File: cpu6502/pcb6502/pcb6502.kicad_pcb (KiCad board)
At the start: 4 copper layers, 134.6 x 96.5 mm, 38 parts, among them J1 Power, J2 RS232, J3 VIA PA, J4 VIA PB, J5 Ext RST, J6 Address, J7 Data, J8 CPU, J9 Interrupt Enable, SW1 Reset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

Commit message: forgot to save previous
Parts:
- removed J9: Interrupt Enable, Connector_PinHeader_2.54mm:PinHeader_2x06_P2.54mm_Vertical
- added SW2: IRQ Enable, Button_Switch_THT:SW_DIP_SPSTx06_Slide_6.7x16.8mm_W7.62mm_P2.54mm_LowProfile, F.Cu at (63.5, 55.9)
- U1: value 6502 (CPU) -> 6502
- U2: value 28C256 (EEPROM) -> EEPROM (28C256)
- U3: value 62256 (RAM) -> RAM (62256)
- U4: value 6522 (VIA) -> VIA (6522)
- U7: value 6551 (UART) -> ACIA (6551)
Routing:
- net /IRQ: track 55.8 -> 51.2 mm
- net /ExtNMI: track 16.2 -> 19.8 mm
- net /ExtIRQ: track 13.7 -> 16.3 mm
- net /VIAIRQ: track 81.2 -> 78.9 mm, vias 1 -> 0
- net /NMI: track 38.3 -> 36.1 mm
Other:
- board text added: "EXT"
- board text added: "Off"
- board text removed: "Ext IRQ"
- board text removed: "Ext NMI"
- board text removed: "Jmp Required for IRQ and NMI"
- board text removed: "No IRQ"
- board text removed: "No NMI"

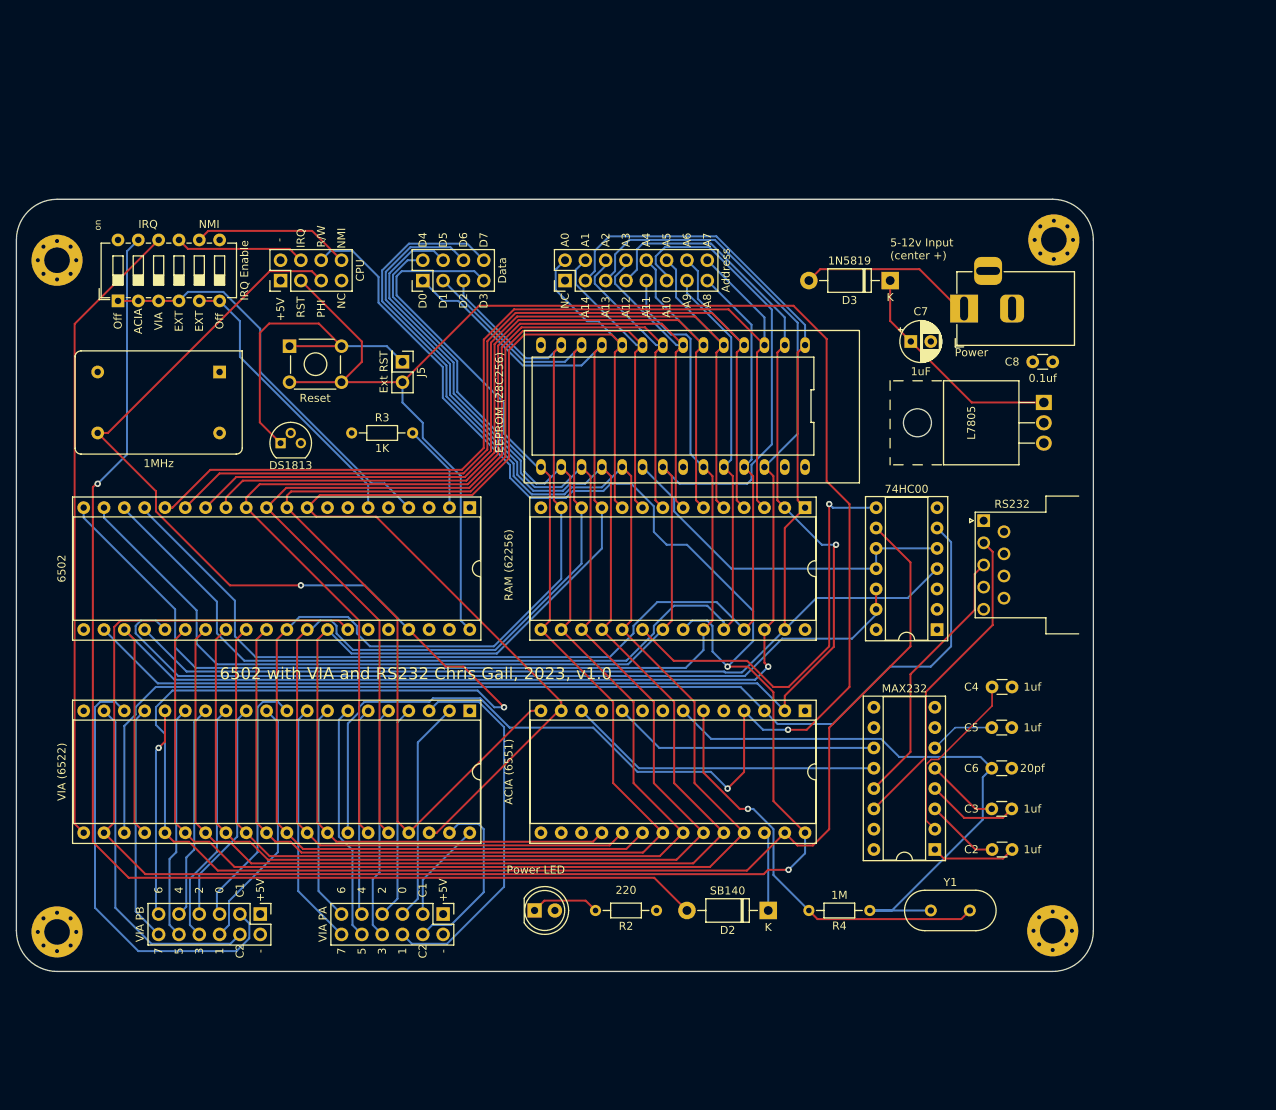
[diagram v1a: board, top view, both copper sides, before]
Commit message: pcb 6502 from 4 layers to 2 layers
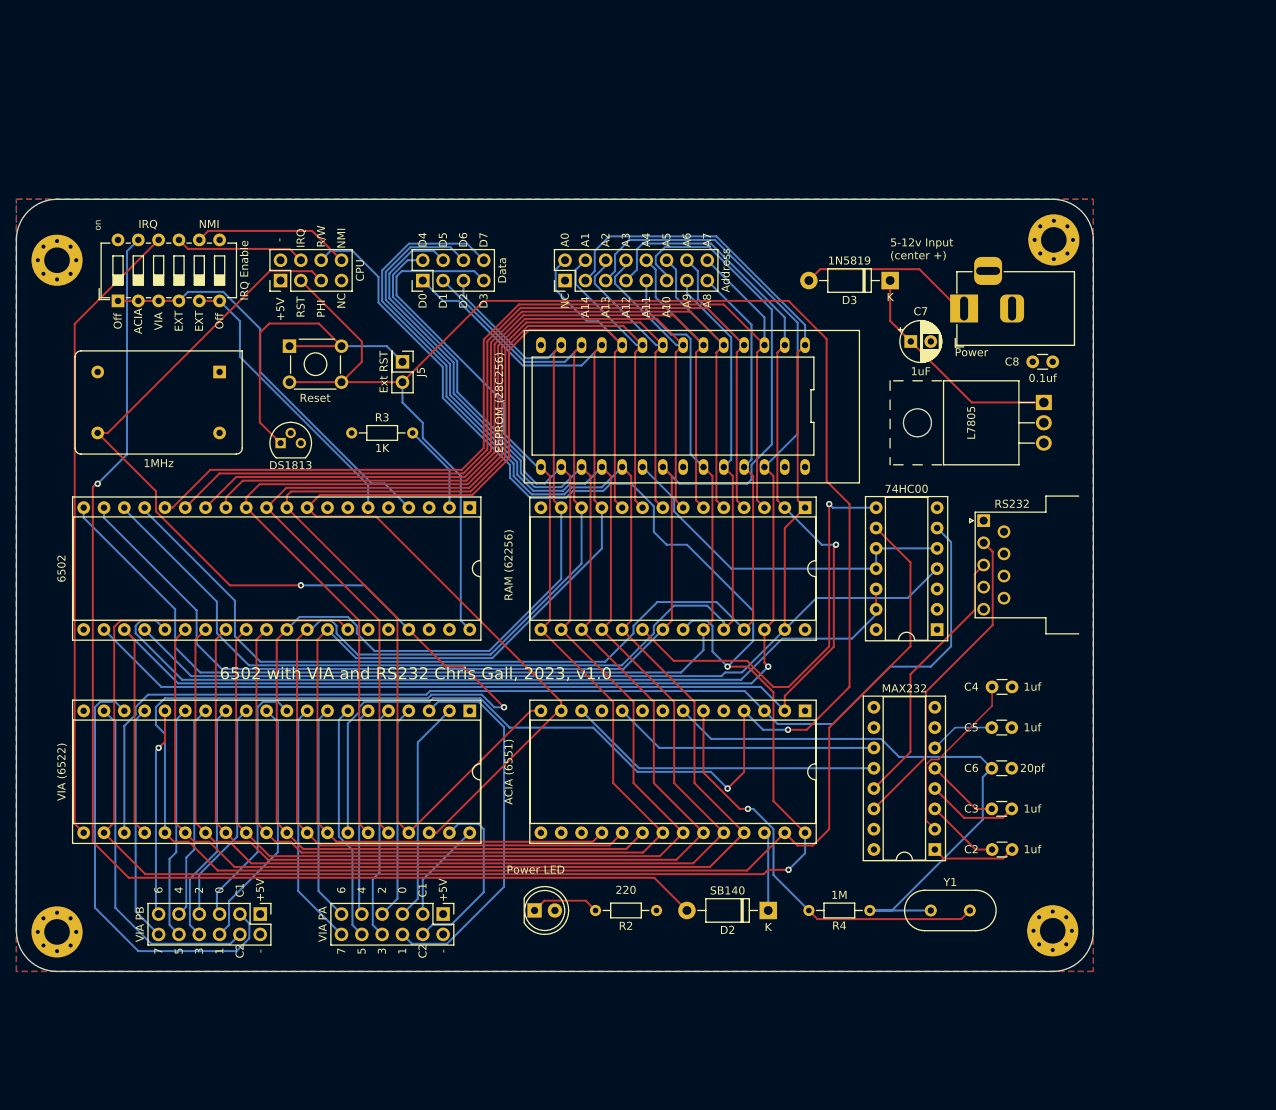
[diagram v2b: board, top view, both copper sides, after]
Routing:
- net /A3: track 157.1 -> 157.6 mm
- net /A7: track 129.6 -> 130.1 mm
- net /A4: track 114.0 -> 114.5 mm
- net /A2: track 150.9 -> 151.5 mm
- net /A0: track 159.0 -> 159.5 mm
- net /A5: track 118.7 -> 119.2 mm
- net /RST: track 263.2 -> 263.7 mm
- net /A6: track 124.2 -> 124.7 mm
- net /A1: track 169.0 -> 169.5 mm
- added copper zone on B.Cu, net +5V
- added copper zone on F.Cu, net GND
- removed copper zone on In2.Cu, net +5V
- removed copper zone on In1.Cu, net GND
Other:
- copper layers 4 -> 2

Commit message: PCB: Add RS232 RCV LED, get pours connected, CODE: checkpoint
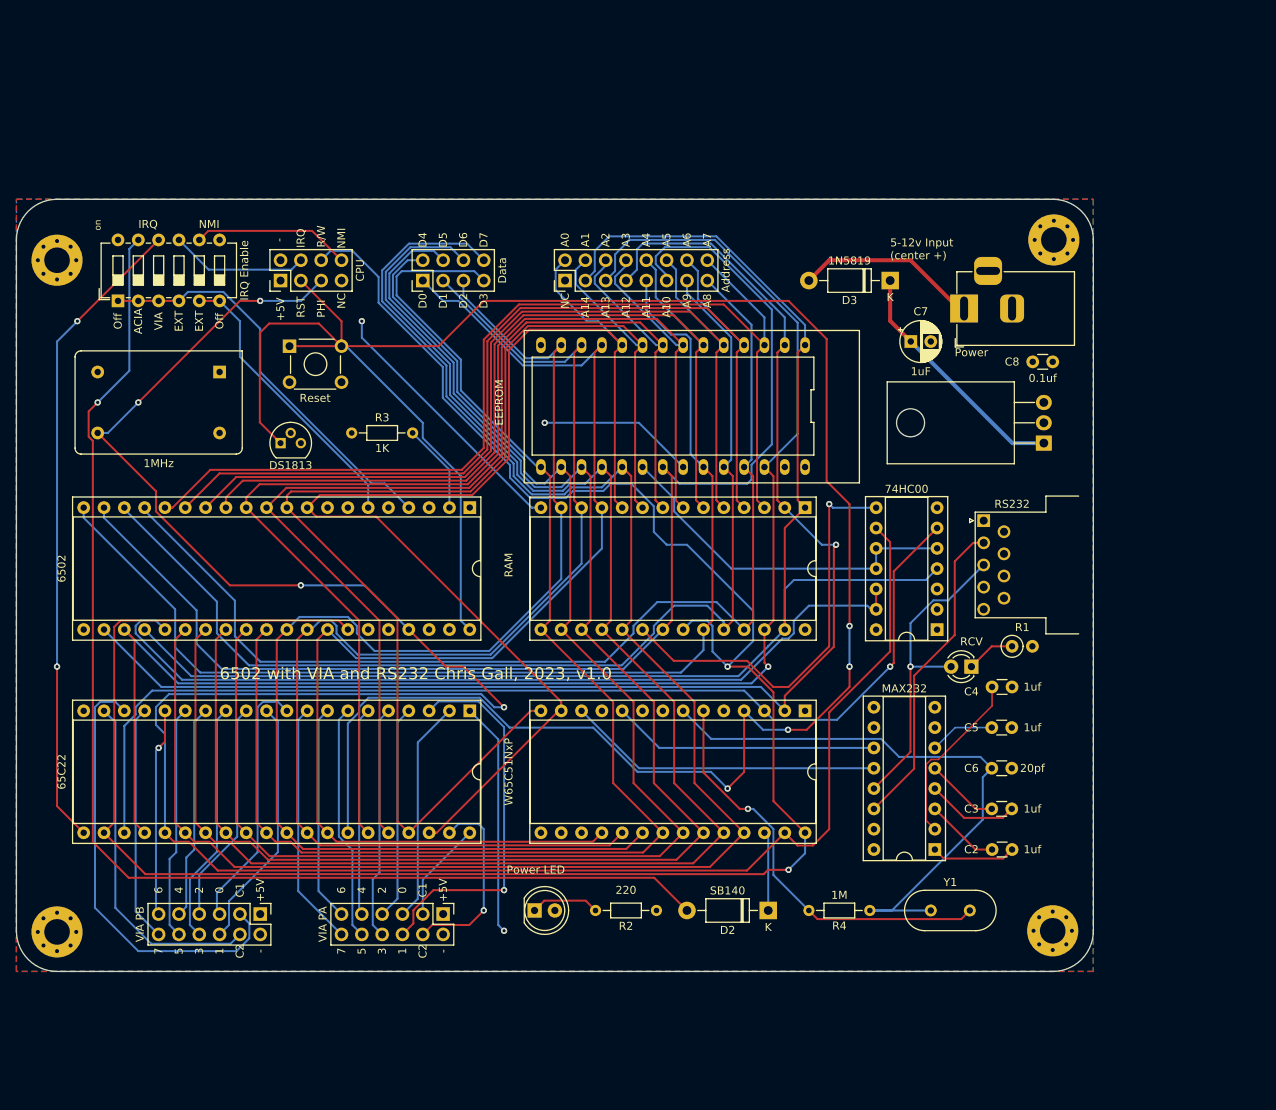
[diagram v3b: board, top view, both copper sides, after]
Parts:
- removed J5: Ext RST, Connector_PinHeader_2.54mm:PinHeader_2x01_P2.54mm_Vertical
- added D4: RCV, LED_THT:LED_D3.0mm, F.Cu at (170.2, 101.6)
- added R1: 220, Resistor_THT:R_Axial_DIN0207_L6.3mm_D2.5mm_P2.54mm_Vertical, F.Cu at (175.3, 99.1)
- U2: value EEPROM (28C256) -> EEPROM
- U3: value RAM (62256) -> RAM
- U4: value VIA (6522) -> 65C22
- U6: footprint Package_TO_SOT_THT:TO-220F-3_Horizontal_TabUp -> Package_TO_SOT_THT:TO-220-3_Horizontal_TabDown
- U7: value ACIA (6551) -> W65C51NxP
- moved U6 5.08 mm to (179.2, 73.7), turned to 90 degrees
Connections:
- SW1 pad 1: Net-(J5-Pin_1) -> /RST
- SW1 pad 2: /RST -> GND
- U9 pad 1: Net-(J5-Pin_1) -> /RST
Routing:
- net GND: track 0.00 -> 82.1 mm, vias 0 -> 3
- net Net-(J5-Pin_1): track 41.7 -> 0.00 mm
- net /RST: track 263.7 -> 290.1 mm, vias 2 -> 4
- net Net-(D4-A): track 33.6 -> 39.8 mm, vias 0 -> 1
- net Net-(D4-K): track 0.00 -> 6.13 mm
- net /CS2: track 140.3 -> 135.5 mm, vias 0 -> 1
- net /PHI2: track 296.3 -> 293.3 mm, vias 2 -> 4
- net /A14: track 182.8 -> 185.7 mm
- net Net-(D3-K): track 28.5 -> 30.6 mm
- net /A15: track 106.9 -> 108.7 mm
- net /VIAIRQ: track 78.9 -> 80.7 mm, vias 0 -> 2
- net /CA2: track 22.7 -> 24.1 mm, vias 0 -> 1
- net /ExtIRQ: track 16.3 -> 17.3 mm
- net Net-(D3-A): track 22.0 -> 23.0 mm
- net /PA1: track 47.2 -> 47.5 mm, vias 0 -> 1

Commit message: tweaks
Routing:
- net /XTAL2: track 74.7 -> 70.1 mm
- net /A15: track 108.7 -> 111.4 mm
- net /R/W: track 276.1 -> 275.3 mm

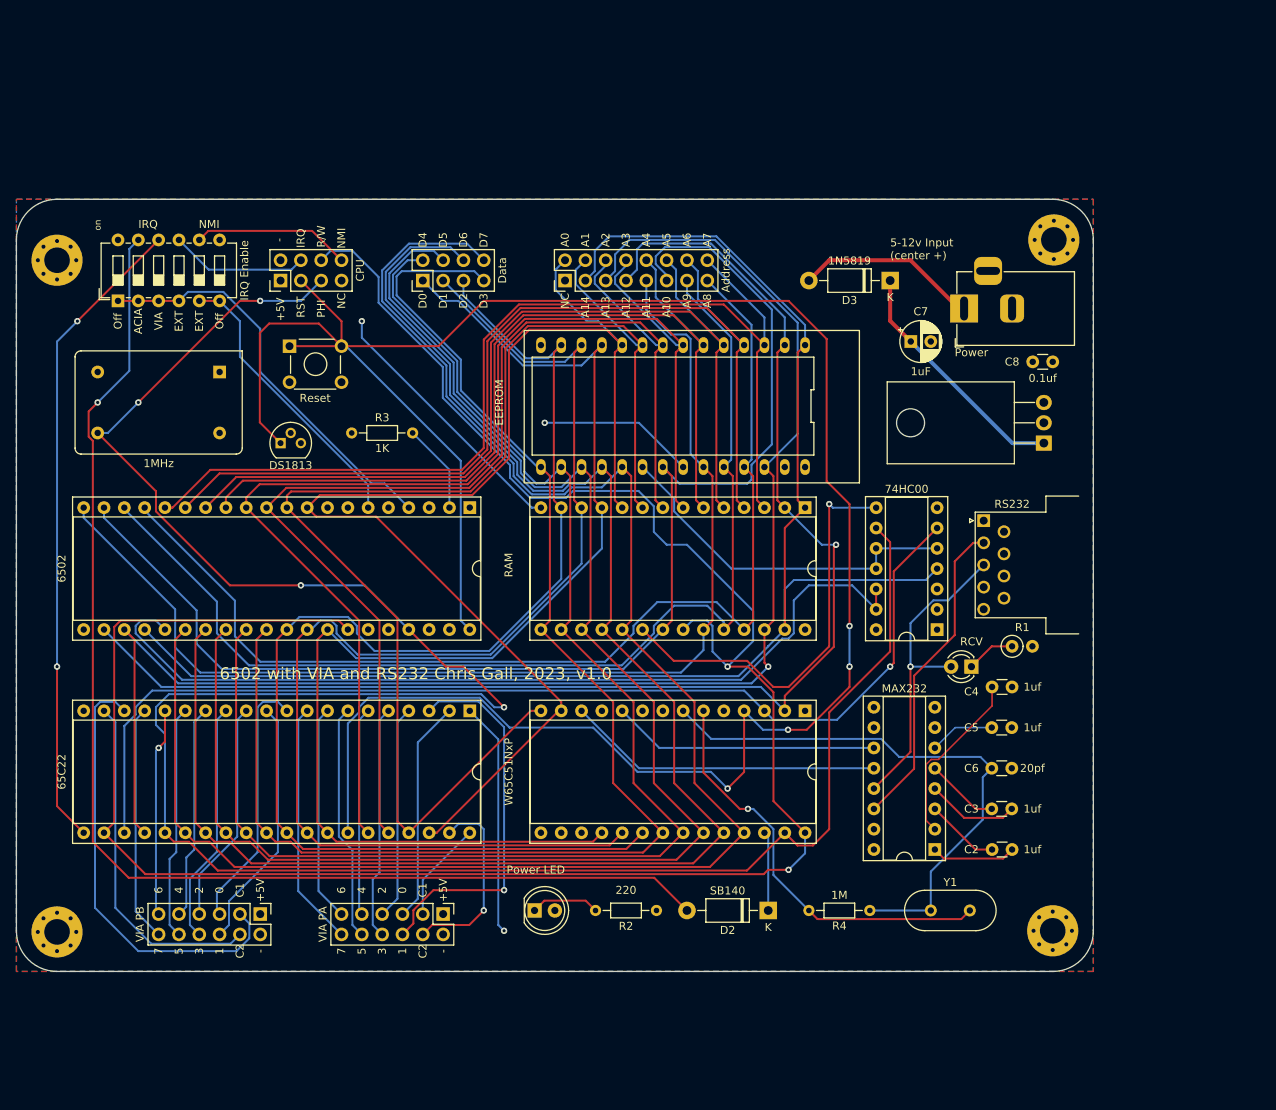
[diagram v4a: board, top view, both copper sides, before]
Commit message: update PCB with debug button, other cleanup, add Wozmon to cgOS and get it working!
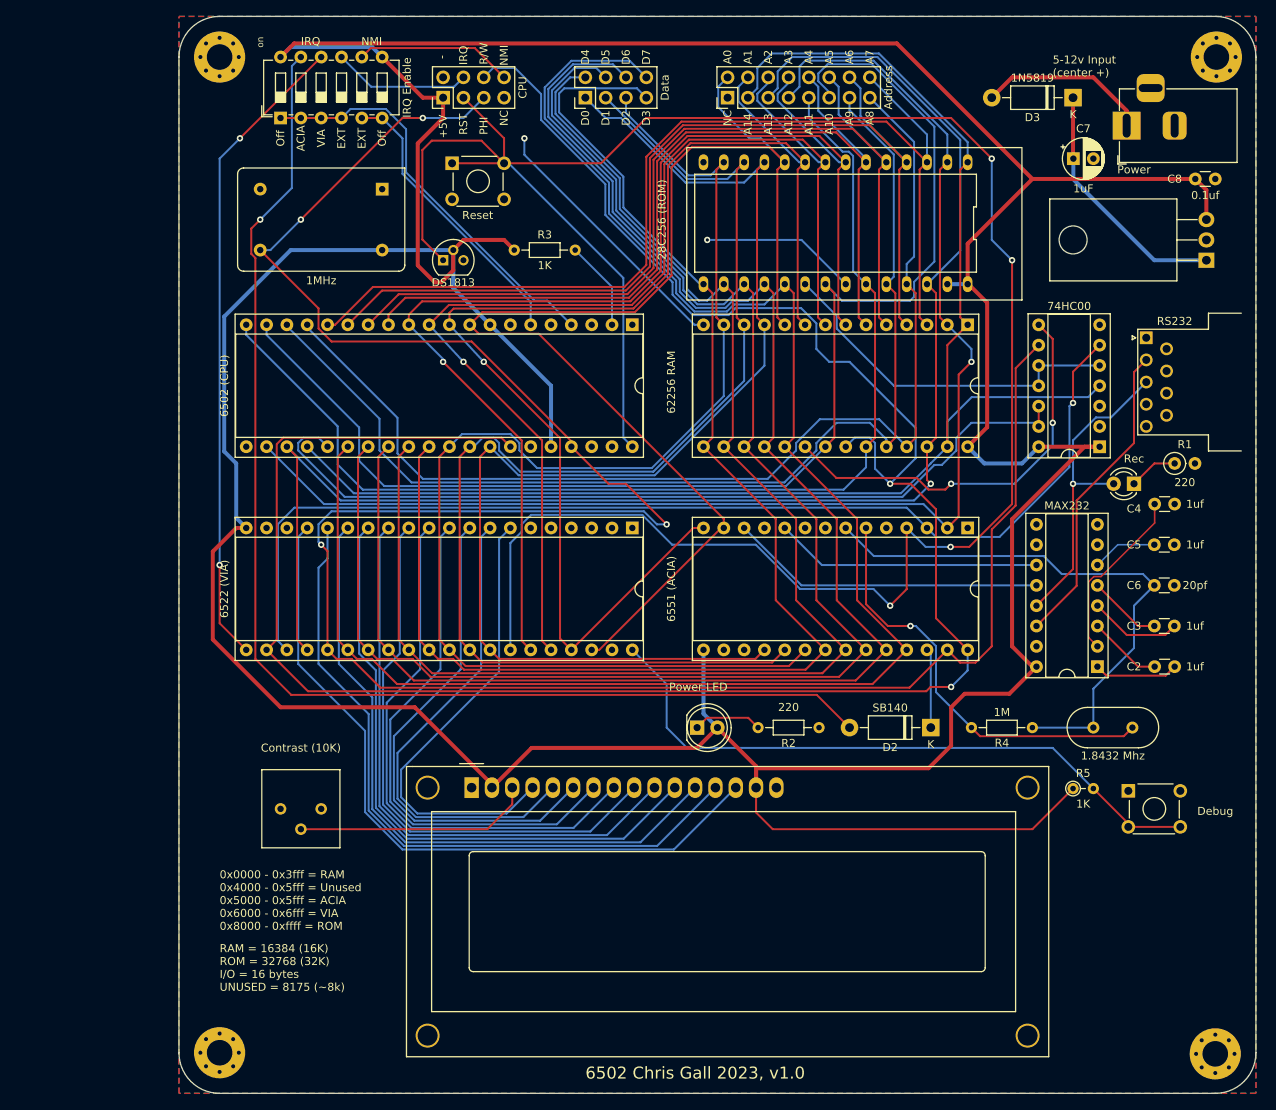
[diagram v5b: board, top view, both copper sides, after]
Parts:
- removed J3: VIA PA, Connector_PinHeader_2.54mm:PinHeader_2x06_P2.54mm_Vertical
- removed J4: VIA PB, Connector_PinHeader_2.54mm:PinHeader_2x06_P2.54mm_Vertical
- added DS1: HY1602E, Display:WC1602A, F.Cu at (107.7, 116.7)
- added R5: 1K, Resistor_THT:R_Axial_DIN0204_L3.6mm_D1.6mm_P2.54mm_Vertical, F.Cu at (182.9, 116.8)
- added RV1: Contrast (10K), Potentiometer_THT:Potentiometer_Bourns_3386P_Vertical, F.Cu at (83.8, 119.4)
- added SW3: Debug, Button_Switch_THT:SW_TH_Tactile_Omron_B3F-10xx, F.Cu at (189.8, 117.1)
- D4: value RCV -> Rec
- U1: value 6502 -> 6502 (CPU)
- U2: value EEPROM -> 28C256 (ROM)
- U3: value RAM -> 62256 RAM
- U4: value 65C22 -> 6522 (VIA)
- U7: value W65C51NxP -> 6551 (ACIA)
- Y1: value Crystal -> 1.8432 Mhz
- moved H2 32.5 mm to (76.2, 25.4)
- moved D3 32.3 mm to (182.9, 30.5)
- moved R4 30.6 mm to (177.8, 109.2)
- moved U3 30.6 mm to (169.7, 58.9)
- moved C2 30.6 mm to (195.6, 101.6)
- moved C4 30.6 mm to (195.6, 81.3)
- moved H1 30.6 mm to (200.8, 25.4)
- moved J1 30.6 mm to (189.6, 34.0)
- moved R1 30.6 mm to (195.6, 76.2)
- moved U5 30.6 mm to (186.2, 74.1)
- moved U6 30.6 mm to (199.6, 50.8)
- moved U7 30.6 mm to (169.7, 84.3)
- moved J2 30.6 mm to (192.0, 60.5)
- moved J7 30.6 mm to (121.9, 30.5)
- moved J8 30.6 mm to (104.1, 30.5)
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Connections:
- J1 pad 3: (no net) -> unconnected-(J1-Pad3)
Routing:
- net +5V: track 0.00 -> 575.9 mm
- net /CA1: track 12.6 -> 81.1 mm
- net /PB7: track 29.6 -> 90.9 mm
- net /PB6: track 26.0 -> 86.6 mm, vias 1 -> 0
- net /CB1: track 55.2 -> 0.00 mm
- net /PB5: track 29.2 -> 82.2 mm
- net /PB4: track 26.8 -> 77.9 mm
- net /PA1: track 47.5 -> 0.00 mm, vias 1 -> 0
- net /PB3: track 30.3 -> 73.6 mm
- net /CB2: track 43.1 -> 0.00 mm
- net /PB2: track 27.8 -> 71.0 mm
- net /PB1: track 31.5 -> 68.4 mm
- net /PA6: track 27.1 -> 60.5 mm
- net /PB0: track 32.5 -> 65.8 mm
- net /PA7: track 30.7 -> 63.1 mm
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- added copper zone on B.Cu, net GND
- removed copper zone on B.Cu, net +5V
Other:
- board size 134.6 x 96.5 mm -> 134.6 x 134.6 mm
- board text added: "0x0000 - 0x3fff = RAM 0x4000 - 0x5fff = Unused 0x5000 - 0x5fff = ACIA 0x6000 - 0x6fff = VIA 0x8000 - 0xffff = ROM"
- board text added: "6502 Chris Gall 2023, v1.0"
- board text added: "RAM = 16384 (16K) ROM = 32768 (32K) I/O = 16 bytes UNUSED = 8175 (~8k)"
- board text removed: "0"
- board text removed: "1"
- board text removed: "2"
- board text removed: "3"
- board text removed: "4"
- board text removed: "5"
- board text removed: "6"
- board text removed: "6502 with VIA and RS232 Chris Gall, 2023, v1.0"
- board text removed: "7"
- board text removed: "C1"
- board text removed: "C2"

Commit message: code changes (wip), set test PCB 2.0 to PCBway
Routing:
- net Net-(D3-A): track 21.5 -> 25.1 mm
- net +5V: track 575.9 -> 576.7 mm
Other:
- board text added: "Power 6-12v Input (center +)"
- board text removed: "5-12v Input (center +)"
